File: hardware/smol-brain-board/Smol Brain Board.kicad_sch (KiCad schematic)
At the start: 61 parts, among them J1 USB_C_Receptacle, J3 CAN_DBG, J6 Smol_Brain_Board, J7 PROGRAM, U1 ESP32-S3-WROOM-1-N8, U2 TCAN3414

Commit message: Fixed footprint mismatch
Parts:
- CRX1, CTX1: footprint LED_SMD:LED_0402_1005Metric -> LED_SMD:LED_0603_1608Metric
- D1, D4: footprint Diode_SMD:D_SOD-323F -> Diode_SMD:D_SOD-123F
- J1: footprint Connector_USB:USB_C_Receptacle_Amphenol_12401610E4-2A -> Connector_USB:USB_C_Receptacle_Amphenol_12401548E4-2A
- R5, R7: distributors part number 311-1KMTR-ND -> RMCF0603FT1K00TR-ND; manufactuer part number RC0201FR-071KL -> RMCF0603FT1K00; manufacturer YAGEO -> Stackpole Electronics Inc
- STATUS1: value WS2812B -> 16347
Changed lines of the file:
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@@
 			)
 		)
-		(property "manufacturer" "YAGEO"
+		(property "manufacturer" "Stackpole Electronics Inc"
 			(at 336.55 29.21 90)
 			(effects
@@
 			)
 		)
-		(property "distributors part number" "311-1KMTR-ND"
+		(property "distributors part number" "RMCF0603FT1K00TR-ND"
 			(at 336.55 29.21 90)
 			(effects
@@
 			)
 		)
-		(property "manufactuer part number" "RC0201FR-071KL"
+		(property "manufactuer part number" "RMCF0603FT1K00"
 			(at 336.55 29.21 90)
 			(effects
@@
 			)
 		)
-		(property "Footprint" "Diode_SMD:D_SOD-323F"
+		(property "Footprint" "Diode_SMD:D_SOD-123F"
 			(at 121.92 147.32 0)
 			(effects
@@
 			)
 		)
-		(property "Footprint" "LED_SMD:LED_0402_1005Metric"
+		(property "Footprint" "LED_SMD:LED_0603_1608Metric"
 			(at 270.51 194.31 0)
 			(effects
@@
 			)
 		)
-		(property "manufacturer" "YAGEO"
+		(property "manufacturer" "Stackpole Electronics Inc"
 			(at 336.55 31.75 90)
 			(effects
@@
 			)
 		)
-		(property "distributors part number" "311-1KMTR-ND"
+		(property "distributors part number" "RMCF0603FT1K00TR-ND"
 			(at 336.55 31.75 90)
 			(effects
@@
 			)
 		)
-		(property "manufactuer part number" "RC0201FR-071KL"
+		(property "manufactuer part number" "RMCF0603FT1K00"
 			(at 336.55 31.75 90)
 			(effects
@@
 					(size 1.27 1.27)
 				)
+				(hide yes)
 			)
 		)
@@
 					(size 1.27 1.27)
 				)
+				(hide yes)
 			)
 		)
-		(property "Footprint" "Connector_USB:USB_C_Receptacle_Amphenol_12401610E4-2A"
+		(property "Footprint" "Connector_USB:USB_C_Receptacle_Amphenol_12401548E4-2A"
 			(at 147.32 63.5 0)
 			(effects
@@
 			)
 		)
-		(property "Value" "WS2812B"
+		(property "Value" "16347"
 			(at 369.57 107.95 0)
 			(effects
@@
 			)
 		)
-		(property "Footprint" "LED_SMD:LED_0402_1005Metric"
+		(property "Footprint" "LED_SMD:LED_0603_1608Metric"
 			(at 278.13 194.31 0)
 			(effects
@@
 			)
 		)
-		(property "Footprint" "Diode_SMD:D_SOD-323F"
+		(property "Footprint" "Diode_SMD:D_SOD-123F"
 			(at 121.92 152.4 0)
 			(effects

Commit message: Swapped pos and neg data lines, finalised design.
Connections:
- net uC_USB_D_N: now also U1.13 (USB_D-); no longer JP2.1 (A), U1.14 (USB_D+)
- net uC_USB_D_P: now also U1.14 (USB_D+); no longer JP1.1 (A), U1.13 (USB_D-)
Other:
- moved on the sheet: JP1, JP2
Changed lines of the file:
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@@
 	(wire
 		(pts
-			(xy 359.41 45.72) (xy 345.44 45.72)
+			(xy 359.41 48.26) (xy 345.44 48.26)
 		)
 		(stroke
@@
 	(wire
 		(pts
-			(xy 228.6 185.42) (xy 228.6 187.96)
+			(xy 322.58 45.72) (xy 336.55 45.72)
 		)
 		(stroke
@@
 	(wire
 		(pts
-			(xy 143.51 104.14) (xy 149.86 104.14)
+			(xy 228.6 185.42) (xy 228.6 187.96)
 		)
 		(stroke
@@
 	(wire
 		(pts
-			(xy 158.75 58.42) (xy 186.69 58.42)
+			(xy 143.51 104.14) (xy 149.86 104.14)
 		)
 		(stroke
@@
 	(wire
 		(pts
-			(xy 293.37 157.48) (xy 293.37 180.34)
+			(xy 158.75 58.42) (xy 186.69 58.42)
 		)
 		(stroke
@@
 	(wire
 		(pts
-			(xy 327.66 36.83) (xy 327.66 43.18)
+			(xy 293.37 157.48) (xy 293.37 180.34)
 		)
 		(stroke
@@
 	(wire
 		(pts
-			(xy 283.21 71.12) (xy 292.1 71.12)
+			(xy 327.66 36.83) (xy 327.66 43.18)
 		)
 		(stroke
@@
 	(wire
 		(pts
-			(xy 322.58 45.72) (xy 337.82 45.72)
+			(xy 283.21 71.12) (xy 292.1 71.12)
 		)
 		(stroke
@@
 	(wire
 		(pts
-			(xy 359.41 48.26) (xy 345.44 48.26)
+			(xy 359.41 45.72) (xy 345.44 45.72)
 		)
 		(stroke
@@
 	(wire
 		(pts
+			(xy 322.58 48.26) (xy 336.55 48.26)
+		)
+		(stroke
+			(width 0)
+			(type default)
+		)
+	)
+	(wire
+		(pts
 			(xy 344.17 55.88) (xy 344.17 62.23)
 		)
@@
 	(wire
 		(pts
-			(xy 322.58 48.26) (xy 337.82 48.26)
-		)
-		(stroke
-			(width 0)
-			(type default)
-		)
-	)
-	(wire
-		(pts
 			(xy 64.77 180.34) (xy 77.47 180.34)
 		)
@@
 	)
 	(label "USB_D_N"
-		(at 359.41 48.26 180)
+		(at 359.41 45.72 180)
 		(fields_autoplaced yes)
 		(effects
@@
 		)
 		(property "Netclass" "USB_DIFF"
-			(at 359.41 49.53 0)
+			(at 359.41 44.45 0)
 			(effects
 				(font
@@
 	)
 	(label "uC_USB_D_P"
-		(at 336.55 45.72 180)
+		(at 336.55 48.26 180)
 		(effects
 			(font
@@
 		)
 		(property "Netclass" "USB_DIFF"
-			(at 337.058 42.672 0)
+			(at 337.058 51.308 0)
 			(effects
 				(font
@@
 	)
 	(label "USB_D_P"
-		(at 359.41 45.72 180)
+		(at 359.41 48.26 180)
 		(fields_autoplaced yes)
 		(effects
@@
 	)
 	(label "uC_USB_D_N"
-		(at 336.55 48.26 180)
+		(at 336.55 45.72 180)
 		(fields_autoplaced yes)
 		(effects
@@
 		)
 		(property "Netclass" "USB_DIFF"
-			(at 336.55 49.53 0)
+			(at 336.55 44.45 0)
 			(effects
 				(font
@@
 	(symbol
 		(lib_id "Jumper:SolderJumper_2_Bridged")
-		(at 341.63 48.26 0)
+		(at 341.63 45.72 0)
+		(mirror x)
 		(unit 1)
 		(exclude_from_sim no)
@@
 		(dnp no)
 		(property "Reference" "JP2"
-			(at 344.424 47.244 0)
+			(at 344.424 46.736 0)
 			(effects
 				(font
@@
 		)
 		(property "Value" "SolderJumper_2_Bridged"
-			(at 341.63 44.45 0)
+			(at 341.63 49.53 0)
 			(effects
 				(font
@@
 		)
 		(property "Footprint" "Jumper:SolderJumper-2_P1.3mm_Bridged_RoundedPad1.0x1.5mm"
-			(at 341.63 48.26 0)
+			(at 341.63 45.72 0)
 			(effects
 				(font
@@
 		)
 		(property "Datasheet" "~"
-			(at 341.63 48.26 0)
+			(at 341.63 45.72 0)
 			(effects
 				(font
@@
 		)
 		(property "Description" "Solder Jumper, 2-pole, closed/bridged"
-			(at 341.63 48.26 0)
+			(at 341.63 45.72 0)
 			(effects
 				(font
@@
 		)
 		(property "manufacturer" "~"
-			(at 341.63 48.26 0)
+			(at 341.63 45.72 0)
 			(effects
 				(font
@@
 		)
 		(property "distributors part number" "~"
-			(at 341.63 48.26 0)
+			(at 341.63 45.72 0)
 			(effects
 				(font
@@
 		)
 		(property "manufactuer part number" "~"
-			(at 341.63 48.26 0)
+			(at 341.63 45.72 0)
 			(effects
 				(font
@@
 	(symbol
 		(lib_id "Jumper:SolderJumper_2_Bridged")
-		(at 341.63 45.72 0)
+		(at 341.63 48.26 0)
+		(mirror x)
 		(unit 1)
 		(exclude_from_sim no)
@@
 		(dnp no)
 		(property "Reference" "JP1"
-			(at 344.424 43.942 0)
+			(at 344.424 50.038 0)
 			(effects
 				(font
@@
 		)
 		(property "Value" "SolderJumper_2_Bridged"
-			(at 341.63 41.91 0)
+			(at 341.63 52.07 0)
 			(effects
 				(font
@@
 		)
 		(property "Footprint" "Jumper:SolderJumper-2_P1.3mm_Bridged_RoundedPad1.0x1.5mm"
-			(at 341.63 45.72 0)
+			(at 341.63 48.26 0)
 			(effects
 				(font
@@
 		)
 		(property "Datasheet" "~"
-			(at 341.63 45.72 0)
+			(at 341.63 48.26 0)
 			(effects
 				(font
@@
 		)
 		(property "Description" "Solder Jumper, 2-pole, closed/bridged"
-			(at 341.63 45.72 0)
+			(at 341.63 48.26 0)
 			(effects
 				(font
@@
 		)
 		(property "manufacturer" "~"
-			(at 341.63 45.72 0)
+			(at 341.63 48.26 0)
 			(effects
 				(font
@@
 		)
 		(property "distributors part number" "~"
-			(at 341.63 45.72 0)
+			(at 341.63 48.26 0)
 			(effects
 				(font
@@
 		)
 		(property "manufactuer part number" "~"
-			(at 341.63 45.72 0)
+			(at 341.63 48.26 0)
 			(effects
 				(font

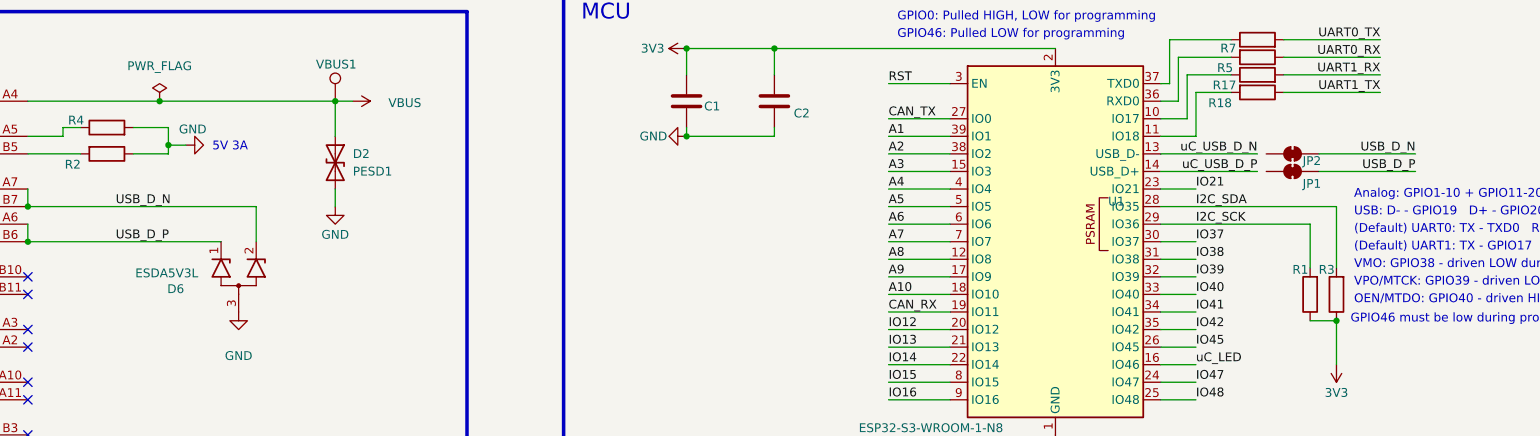
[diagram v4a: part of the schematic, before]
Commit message: Fixed pcb layout to suit previous schematic changes
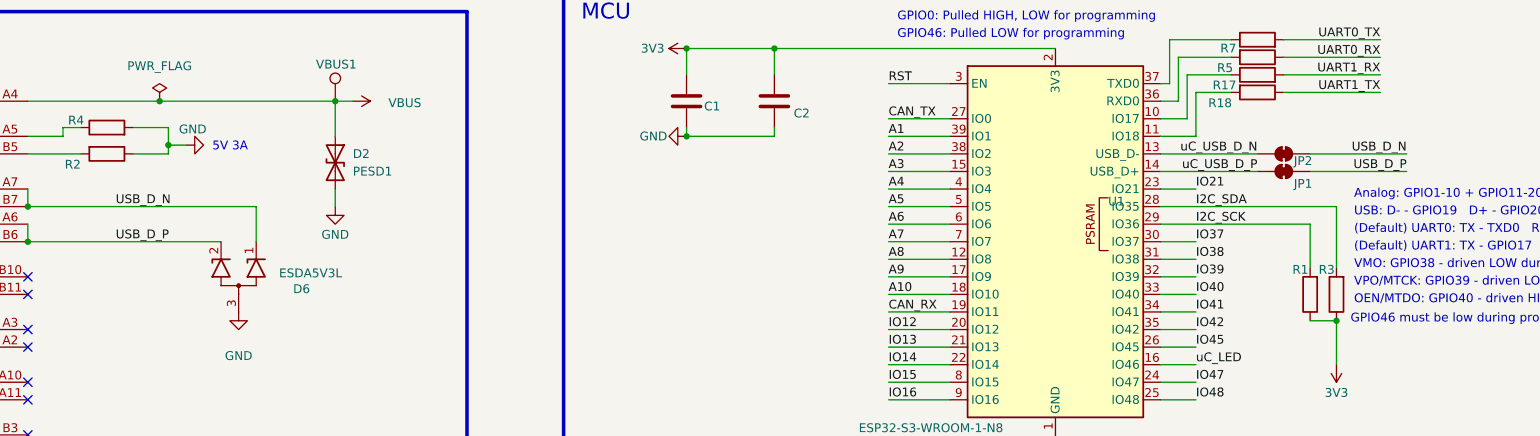
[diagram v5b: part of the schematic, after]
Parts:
- J1: footprint Connector_USB:USB_C_Receptacle_Amphenol_12401548E4-2A -> Connector_USB:USB_C_Receptacle_Amphenol_12401610E4-2A
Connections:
- net USB_D_N: now also D6.1 (K1); no longer D6.2 (K2)
- net USB_D_P: now also D6.2 (K2); no longer D6.1 (K1)
- net uC_USB_D_N: now also JP2.1 (A)
- net uC_USB_D_P: now also JP1.1 (A)
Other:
- moved on the sheet: D6, JP1, JP2
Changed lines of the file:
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@@
 	(wire
 		(pts
-			(xy 359.41 48.26) (xy 345.44 48.26)
+			(xy 358.14 48.26) (xy 344.17 48.26)
 		)
 		(stroke
@@
 	(wire
 		(pts
-			(xy 359.41 45.72) (xy 345.44 45.72)
+			(xy 358.14 45.72) (xy 344.17 45.72)
 		)
 		(stroke
@@
 	)
 	(label "USB_D_N"
-		(at 359.41 45.72 180)
+		(at 358.14 45.72 180)
 		(fields_autoplaced yes)
 		(effects
@@
 		)
 		(property "Netclass" "USB_DIFF"
-			(at 359.41 44.45 0)
+			(at 358.14 44.45 0)
 			(effects
 				(font
@@
 	)
 	(label "USB_D_P"
-		(at 359.41 48.26 180)
+		(at 358.14 48.26 180)
 		(fields_autoplaced yes)
 		(effects
@@
 		)
 		(property "Netclass" "USB_DIFF"
-			(at 359.41 46.99 0)
+			(at 358.14 46.99 0)
 			(effects
 				(font
@@
 	(symbol
 		(lib_id "Jumper:SolderJumper_2_Bridged")
-		(at 341.63 45.72 0)
+		(at 340.36 45.72 0)
 		(mirror x)
 		(unit 1)
@@
 		(dnp no)
 		(property "Reference" "JP2"
-			(at 344.424 46.736 0)
+			(at 343.154 46.736 0)
 			(effects
 				(font
@@
 		)
 		(property "Value" "SolderJumper_2_Bridged"
-			(at 341.63 49.53 0)
+			(at 340.36 49.53 0)
 			(effects
 				(font
@@
 		)
 		(property "Footprint" "Jumper:SolderJumper-2_P1.3mm_Bridged_RoundedPad1.0x1.5mm"
-			(at 341.63 45.72 0)
+			(at 340.36 45.72 0)
 			(effects
 				(font
@@
 		)
 		(property "Datasheet" "~"
-			(at 341.63 45.72 0)
+			(at 340.36 45.72 0)
 			(effects
 				(font
@@
 		)
 		(property "Description" "Solder Jumper, 2-pole, closed/bridged"
-			(at 341.63 45.72 0)
+			(at 340.36 45.72 0)
 			(effects
 				(font
@@
 		)
 		(property "manufacturer" "~"
-			(at 341.63 45.72 0)
+			(at 340.36 45.72 0)
 			(effects
 				(font
@@
 		)
 		(property "distributors part number" "~"
-			(at 341.63 45.72 0)
+			(at 340.36 45.72 0)
 			(effects
 				(font
@@
 		)
 		(property "manufactuer part number" "~"
-			(at 341.63 45.72 0)
+			(at 340.36 45.72 0)
 			(effects
 				(font
@@
 	(symbol
 		(lib_id "Jumper:SolderJumper_2_Bridged")
-		(at 341.63 48.26 0)
+		(at 340.36 48.26 0)
 		(mirror x)
 		(unit 1)
@@
 		(dnp no)
 		(property "Reference" "JP1"
-			(at 344.424 50.038 0)
+			(at 343.154 50.038 0)
 			(effects
 				(font
@@
 		)
 		(property "Value" "SolderJumper_2_Bridged"
-			(at 341.63 52.07 0)
+			(at 340.36 52.07 0)
 			(effects
 				(font
@@
 		)
 		(property "Footprint" "Jumper:SolderJumper-2_P1.3mm_Bridged_RoundedPad1.0x1.5mm"
-			(at 341.63 48.26 0)
+			(at 340.36 48.26 0)
 			(effects
 				(font
@@
 		)
 		(property "Datasheet" "~"
-			(at 341.63 48.26 0)
+			(at 340.36 48.26 0)
 			(effects
 				(font
@@
 		)
 		(property "Description" "Solder Jumper, 2-pole, closed/bridged"
-			(at 341.63 48.26 0)
+			(at 340.36 48.26 0)
 			(effects
 				(font
@@
 		)
 		(property "manufacturer" "~"
-			(at 341.63 48.26 0)
+			(at 340.36 48.26 0)
 			(effects
 				(font
@@
 		)
 		(property "distributors part number" "~"
-			(at 341.63 48.26 0)
+			(at 340.36 48.26 0)
 			(effects
 				(font
@@
 		)
 		(property "manufactuer part number" "~"
-			(at 341.63 48.26 0)
+			(at 340.36 48.26 0)
 			(effects
 				(font
@@
 			)
 		)
-		(property "Footprint" "Connector_USB:USB_C_Receptacle_Amphenol_12401548E4-2A"
+		(property "Footprint" "Connector_USB:USB_C_Receptacle_Amphenol_12401610E4-2A"
 			(at 147.32 63.5 0)
 			(effects
@@
 	(symbol
 		(lib_id "Power_Protection:RCLAMP0502B")
-		(at 189.23 63.5 90)
+		(at 189.23 63.5 270)
+		(mirror x)
 		(unit 1)
 		(exclude_from_sim no)
@@
 		(dnp no)
 		(property "Reference" "D6"
-			(at 181.356 64.516 90)
+			(at 197.104 64.516 90)
 			(effects
 				(font
@@
 		)
 		(property "Value" "ESDA5V3L"
-			(at 183.388 62.23 90)
+			(at 195.072 62.23 90)
 			(effects
 				(font
@@
 		)
 		(property "Footprint" "Package_TO_SOT_SMD:SOT-416"
-			(at 196.85 63.5 0)
+			(at 181.61 63.5 0)
 			(effects
 				(font
@@
 		)
 		(property "Datasheet" "https://www.semtech.com/products/circuit-protection/low-capacitance/rclamp0502b"
-			(at 186.69 62.23 0)
+			(at 191.77 62.23 0)
 			(effects
 				(font
